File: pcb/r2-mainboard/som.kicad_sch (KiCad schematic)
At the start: 14 parts, among them J500 MICRO_SD(TFC-WPAPR-08), J501 BTH-060-01-L-D-A-K-TR, J502 BTH-060-01-L-D-A-K-TR, X500 PCM-071

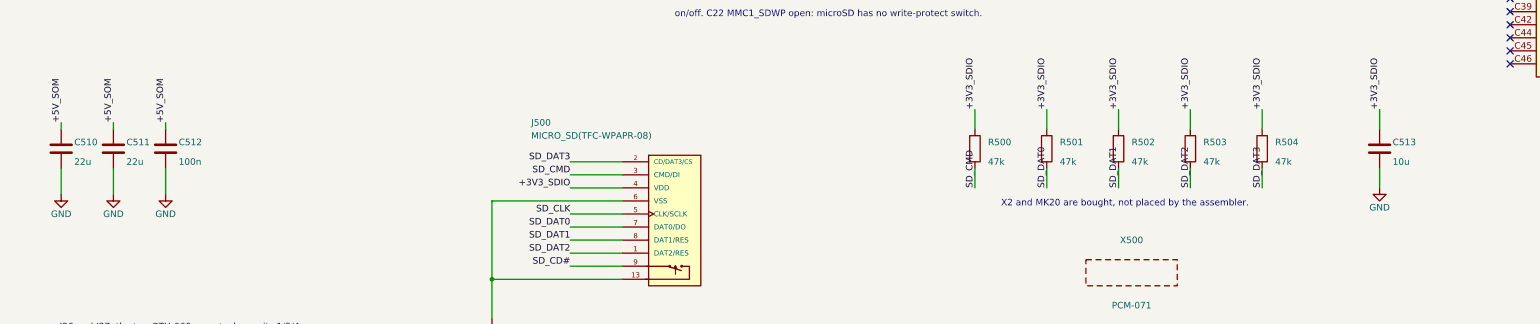
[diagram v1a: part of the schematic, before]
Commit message: Schematics update for new chip.
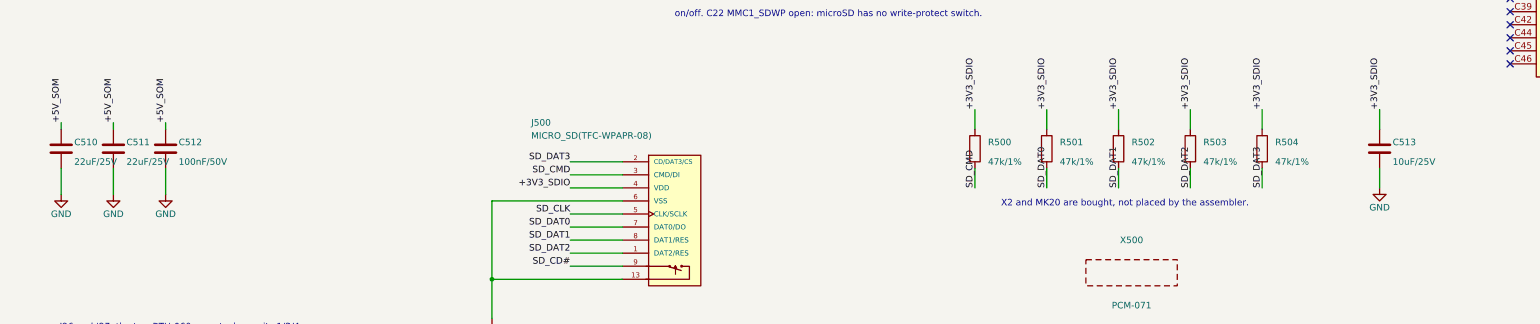
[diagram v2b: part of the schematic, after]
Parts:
- C510, C511: value 22u -> 22uF/25V
- C512: value 100n -> 100nF/50V
- C513: value 10u -> 10uF/25V
- R500, R501, R502, R503, R504: value 47k -> 47k/1%
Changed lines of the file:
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@@
 			)
 		)
-		(property "Value" "47k"
+		(property "Value" "47k/1%"
 			(at 213.36 213.36 0)
 			(show_name no)
@@
 			)
 		)
-		(property "Value" "47k"
+		(property "Value" "47k/1%"
 			(at 269.24 213.36 0)
 			(show_name no)
@@
 			)
 		)
-		(property "Value" "10u"
+		(property "Value" "10uF/25V"
 			(at 292.1 213.36 0)
 			(show_name no)
@@
 			)
 		)
-		(property "Value" "22u"
+		(property "Value" "22uF/25V"
 			(at 35.56 213.36 0)
 			(show_name no)
@@
 			)
 		)
-		(property "Value" "47k"
+		(property "Value" "47k/1%"
 			(at 255.27 213.36 0)
 			(show_name no)
@@
 			)
 		)
-		(property "Value" "47k"
+		(property "Value" "47k/1%"
 			(at 227.33 213.36 0)
 			(show_name no)
@@
 			)
 		)
-		(property "Value" "22u"
+		(property "Value" "22uF/25V"
 			(at 45.72 213.36 0)
 			(show_name no)
@@
 			)
 		)
-		(property "Value" "47k"
+		(property "Value" "47k/1%"
 			(at 241.3 213.36 0)
 			(show_name no)
@@
 			)
 		)
-		(property "Value" "100n"
+		(property "Value" "100nF/50V"
 			(at 55.88 213.36 0)
 			(show_name no)
